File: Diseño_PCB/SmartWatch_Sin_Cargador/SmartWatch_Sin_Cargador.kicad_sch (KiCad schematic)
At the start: 19 parts, among them J1 Input_BAT, J1 Input_Charger, J3 FTDI, SW1 SW_SPST, SW2 SW_Push, SW3 SW_Push, SW4 SW_Push_Dual, SW5 SW_Push_Dual, SW6 SW_Push_Dual, U2 AMS1117-3.3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

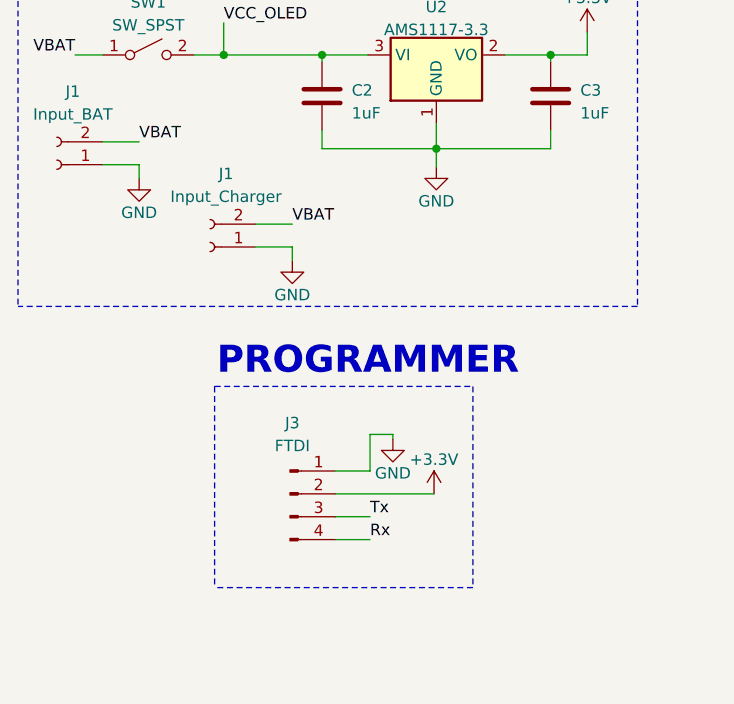
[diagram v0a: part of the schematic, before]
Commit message: Cree las carpetas de diseño 3D y actuaice el PCB del que no lleva cargador
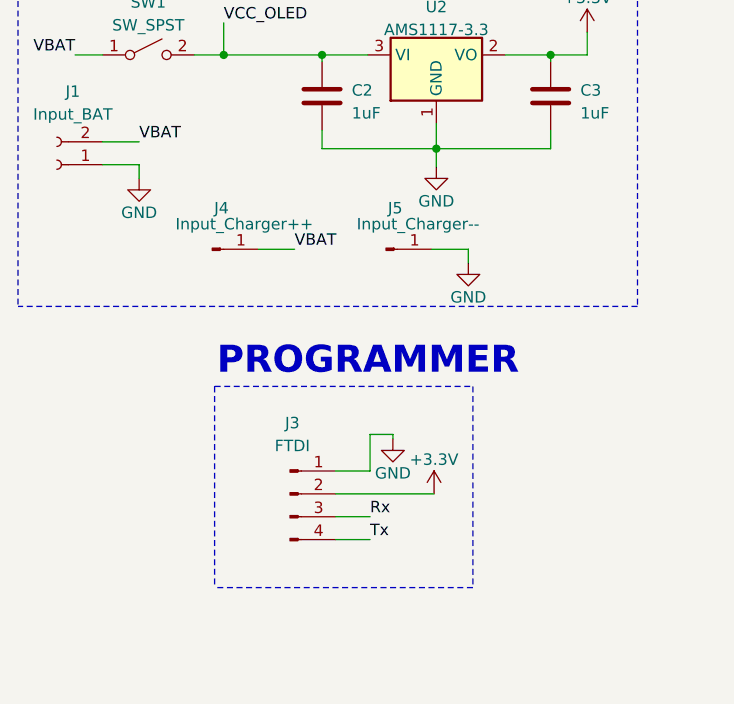
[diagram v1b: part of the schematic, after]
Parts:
- removed J1: Input_Charger, Connector_Wire:SolderWire-0.1sqmm_1x02_P3.6mm_D0.4mm_OD1mm, symbol Connector:Conn_01x02_Socket
- added J4: Input_Charger++, Connector_Wire:SolderWire-0.1sqmm_1x01_D0.4mm_OD1mm, symbol Connector:Conn_01x01_Pin
- added J5: Input_Charger--, Connector_Wire:SolderWire-0.1sqmm_1x01_D0.4mm_OD1mm, symbol Connector:Conn_01x01_Pin
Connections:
- net GND: now also J5.1 (Pin_1)
- net Rx: now also J3.3 (Pin_3); no longer J3.4 (Pin_4)
- net Tx: now also J3.4 (Pin_4); no longer J3.3 (Pin_3)
- net VBAT: now also J4.1 (Pin_1)
